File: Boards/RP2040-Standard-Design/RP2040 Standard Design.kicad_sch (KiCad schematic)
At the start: 2 parts, among them J1 Conn_01x20_Pin, J3 Conn_01x19_Pin

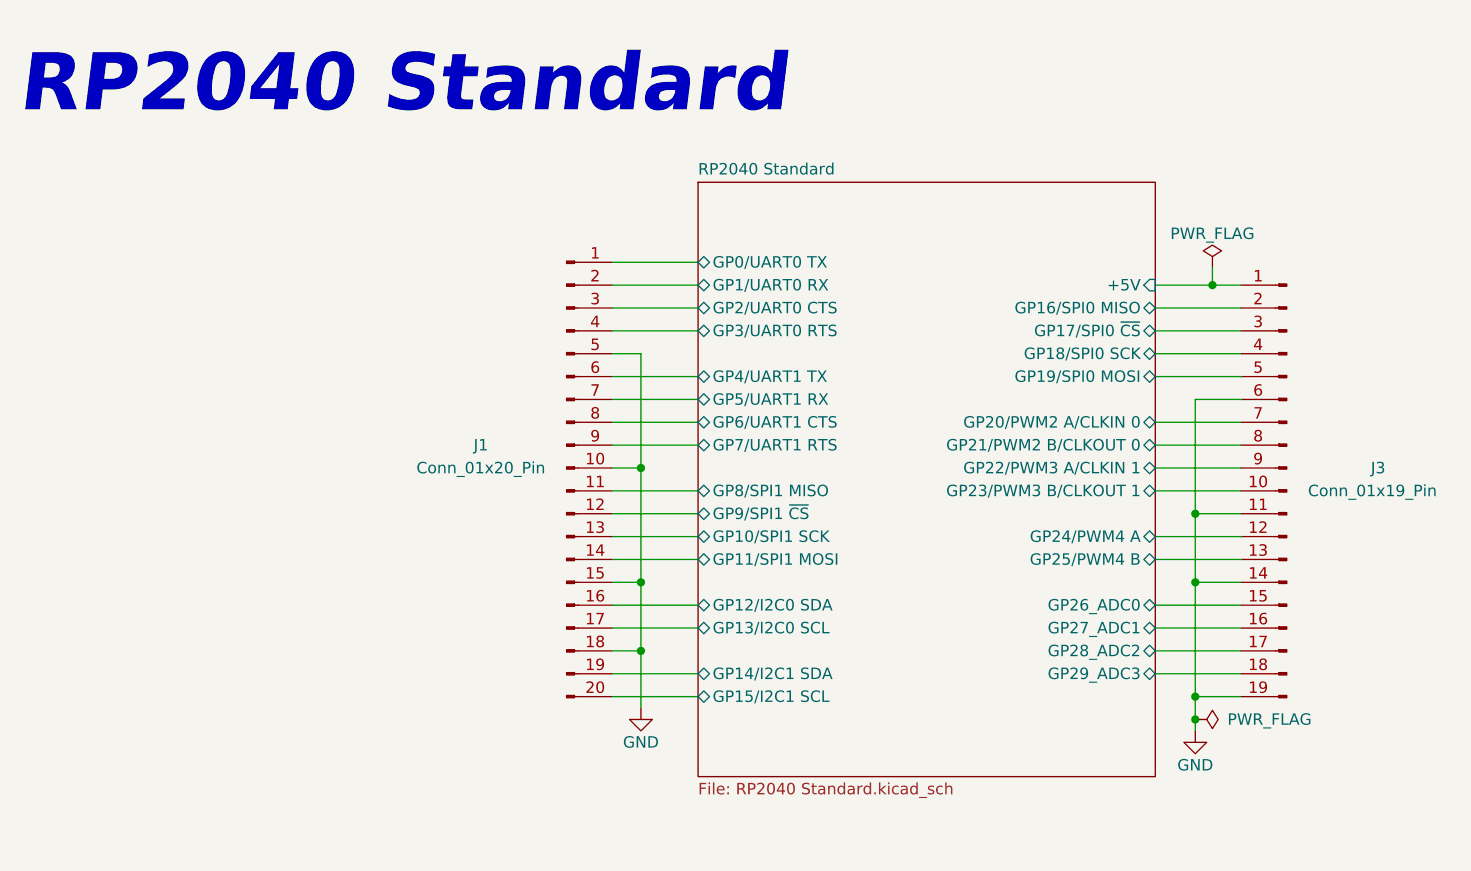
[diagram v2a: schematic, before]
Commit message: changes in RP2040 design
GPIO25 LED is now part of RP2040 Standard
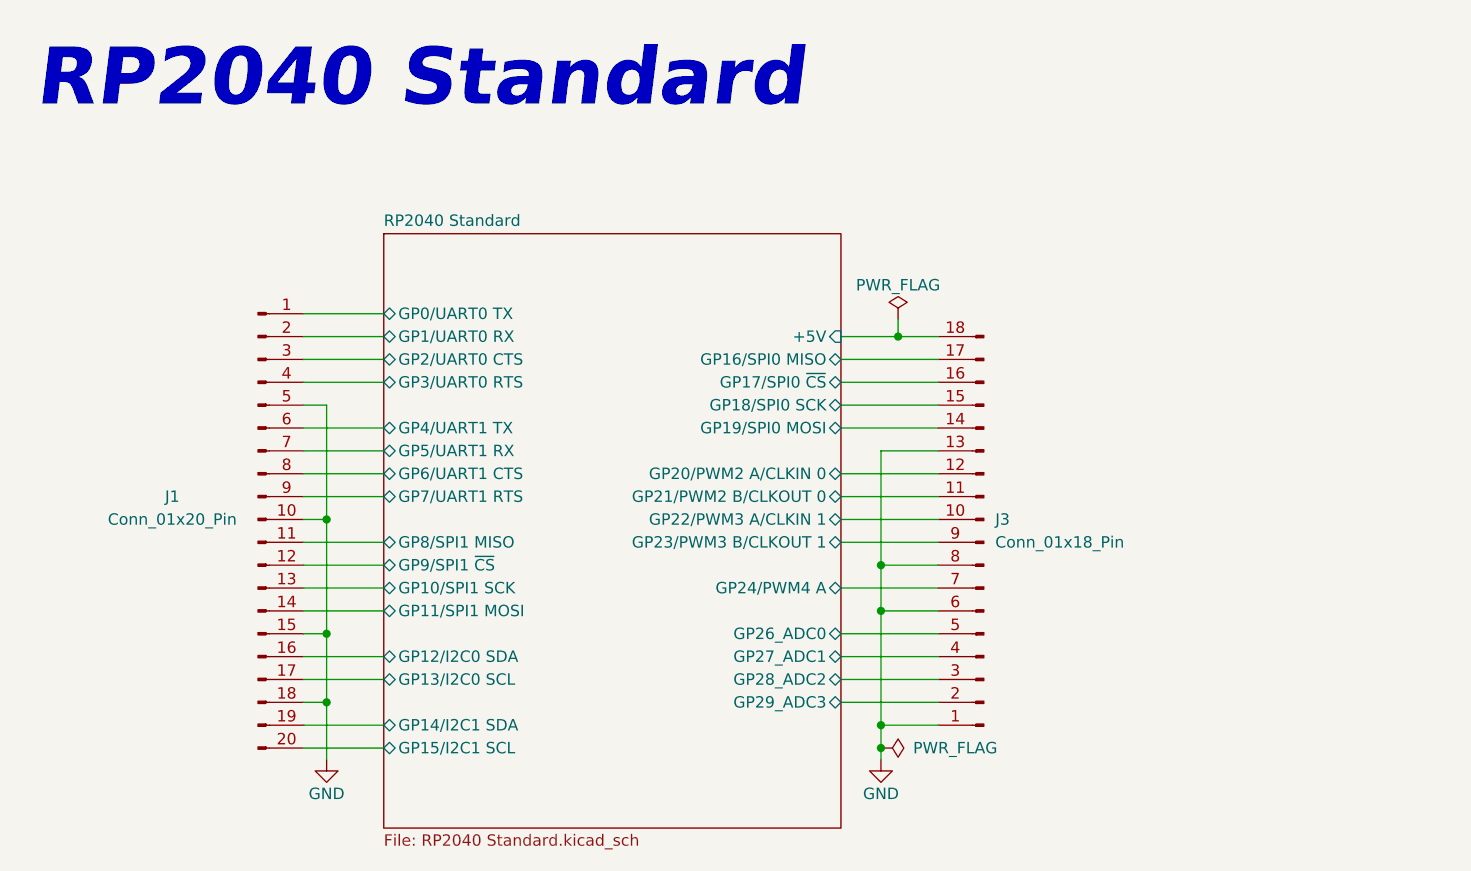
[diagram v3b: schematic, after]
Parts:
- removed J3: Conn_01x19_Pin, symbol Connector:Conn_01x19_Pin
- added J3: Conn_01x18_Pin, symbol Connector:Conn_01x18_Pin
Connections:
- net GND: now also J3.1 (Pin_1), J3.13 (Pin_13), J3.6 (Pin_6), J3.8 (Pin_8)
- net RP2040 Standard/+5V: now also J3.18 (Pin_18)
- net RP2040 Standard/GP16/SPI0 MISO: now also J3.17 (Pin_17)
- net RP2040 Standard/GP17/SPI0 ~{CS}: now also J3.16 (Pin_16)
- net RP2040 Standard/GP18/SPI0 SCK: now also J3.15 (Pin_15)
- net RP2040 Standard/GP19/SPI0 MOSI: now also J3.14 (Pin_14)
- net RP2040 Standard/GP20/PWM2 A/CLKIN 0: now also J3.12 (Pin_12)
- net RP2040 Standard/GP21/PWM2 B/CLKOUT 0: now also J3.11 (Pin_11)
- net RP2040 Standard/GP22/PWM3 A/CLKIN 1: now also J3.10 (Pin_10)
- net RP2040 Standard/GP23/PWM3 B/CLKOUT 1: now also J3.9 (Pin_9)
- net RP2040 Standard/GP24/PWM4 A: now also J3.7 (Pin_7)
- net RP2040 Standard/GP26_ADC0: now also J3.5 (Pin_5)
- net RP2040 Standard/GP27_ADC1: now also J3.4 (Pin_4)
- net RP2040 Standard/GP28_ADC2: now also J3.3 (Pin_3)
- net RP2040 Standard/GP29_ADC3: now also J3.2 (Pin_2)
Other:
- sheet RP2040 Standard ports: added none; removed GP25/PWM4 B
- moved on the sheet: J1
